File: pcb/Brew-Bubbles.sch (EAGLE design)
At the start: 10 parts, among them U1 GP1A57HR, U2 WEMOS-D1-MINI

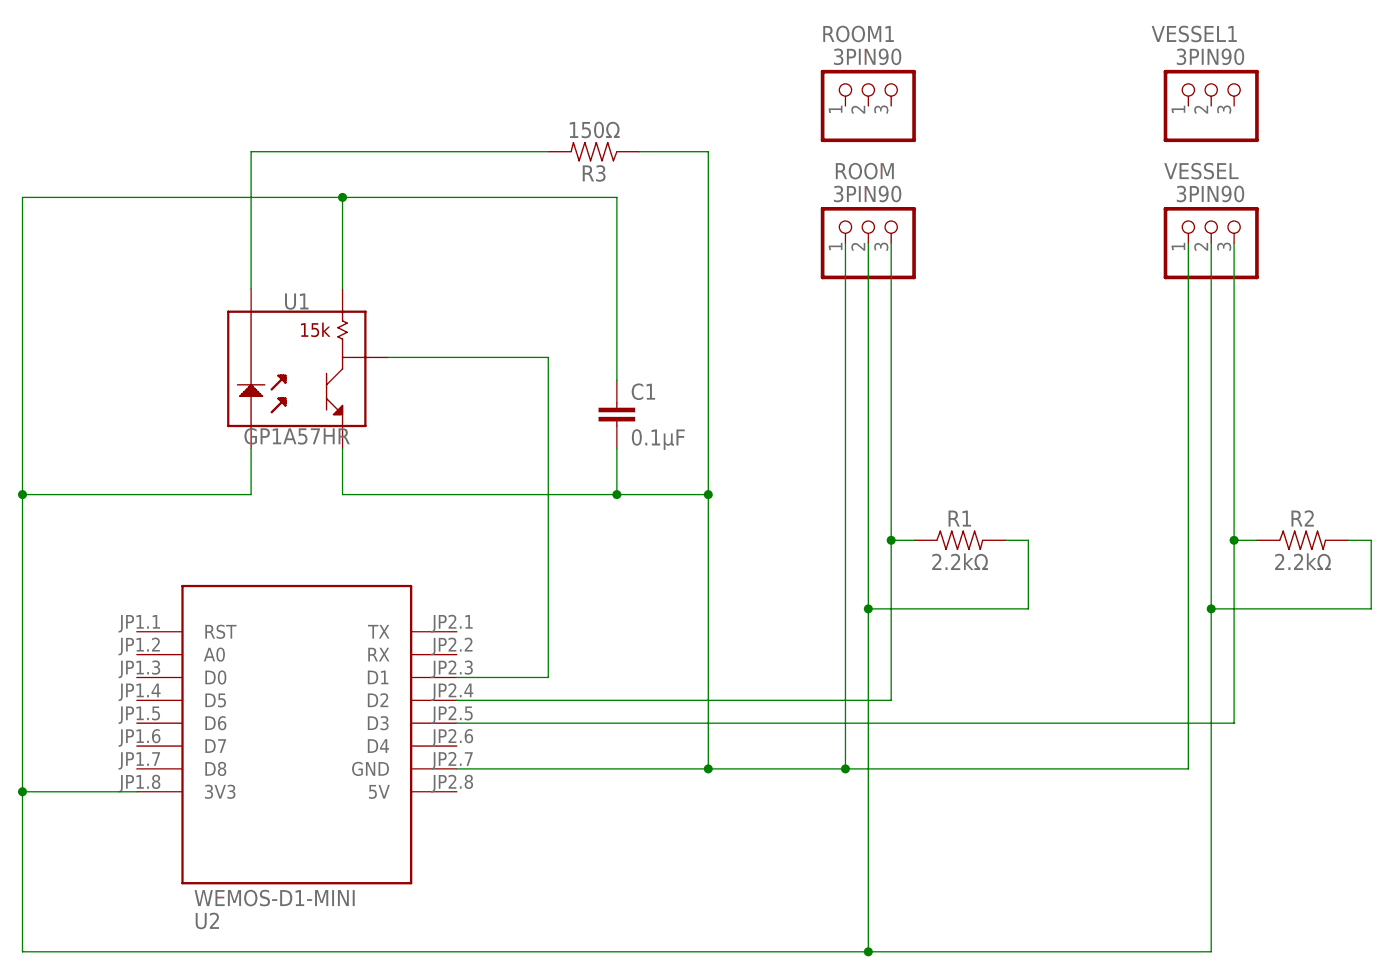
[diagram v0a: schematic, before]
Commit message: Add decoupling caps to 3v3 and 5v
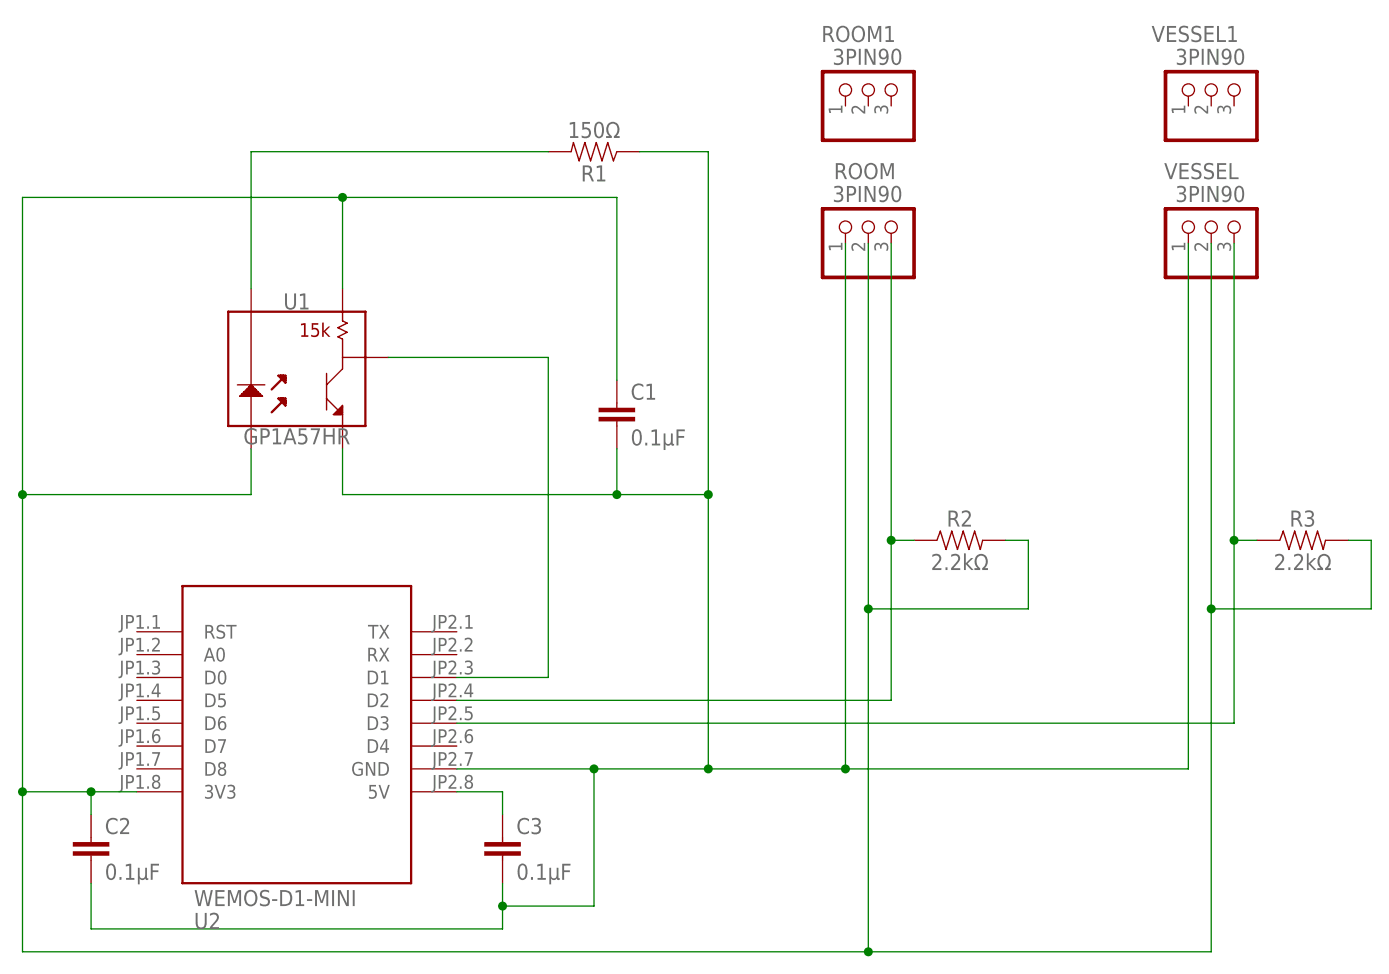
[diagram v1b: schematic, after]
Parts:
- added C2, C3: 0.1μF, rcl:C-EU025-024X044
- R1: value 2.2kΩ -> 150Ω
- R3: value 150Ω -> 2.2kΩ
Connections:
- new net 5V: C3.1, U2.5V
- net 3V3: now also C2.1, R3.2; no longer R1.2
- net D2: now also R2.1; no longer R1.1
- net D3: now also R3.1; no longer R2.1
- net GND: now also C2.2, C3.2, R1.1; no longer R3.1
- net PD1: now also R1.2; no longer R3.2
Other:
- moved on the sheet: R1, R2, R3
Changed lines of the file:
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@@
 <parts>
 <part name="U2" library="diy-modules" deviceset="WEMOS-D1-MINI-SHIELD" device="" value="WEMOS-D1-MINI"/>
-<part name="R1" library="SparkFun-Resistors" deviceset="330OHM" device="-HORIZ-1/10W-5%" value="2.2kΩ"/>
+<part name="R2" library="SparkFun-Resistors" deviceset="330OHM" device="-HORIZ-1/10W-5%" value="2.2kΩ"/>
 <part name="VESSEL" library="pinhead" library_urn="urn:adsk.eagle:library:325" deviceset="PINHD-1X3" device="/90" package3d_urn="urn:adsk.eagle:package:22459/2" value="3PIN90"/>
-<part name="R2" library="SparkFun-Resistors" deviceset="330OHM" device="-HORIZ-1/10W-5%" value="2.2kΩ"/>
+<part name="R3" library="SparkFun-Resistors" deviceset="330OHM" device="-HORIZ-1/10W-5%" value="2.2kΩ"/>
 <part name="U1" library="SparkFun-Sensors" deviceset="GP1A57HR" device=""/>
-<part name="R3" library="SparkFun-Resistors" deviceset="330OHM" device="-HORIZ-1/10W-5%" value="150Ω"/>
+<part name="R1" library="SparkFun-Resistors" deviceset="330OHM" device="-HORIZ-1/10W-5%" value="150Ω"/>
 <part name="ROOM" library="pinhead" library_urn="urn:adsk.eagle:library:325" deviceset="PINHD-1X3" device="/90" package3d_urn="urn:adsk.eagle:package:22459/2" value="3PIN90"/>
 <part name="FRAME1" library="frames" deviceset="LETTER_L" device=""/>
@@
 <part name="VESSEL1" library="pinhead" library_urn="urn:adsk.eagle:library:325" deviceset="PINHD-1X3" device="/90" package3d_urn="urn:adsk.eagle:package:22459/2" value="3PIN90"/>
 <part name="C1" library="rcl" library_urn="urn:adsk.eagle:library:334" deviceset="C-EU" device="025-024X044" package3d_urn="urn:adsk.eagle:package:23630/1" value="0.1μF"/>
+<part name="C3" library="rcl" library_urn="urn:adsk.eagle:library:334" deviceset="C-EU" device="025-024X044" package3d_urn="urn:adsk.eagle:package:23630/1" value="0.1μF"/>
+<part name="C2" library="rcl" library_urn="urn:adsk.eagle:library:334" deviceset="C-EU" device="025-024X044" package3d_urn="urn:adsk.eagle:package:23630/1" value="0.1μF"/>
 </parts>
 <sheets>
@@
 <attribute name="VALUE" x="6.35" y="33.02" size="1.778" layer="96"/>
 </instance>
-<instance part="R1" gate="G$1" x="91.44" y="73.66" smashed="yes">
+<instance part="R2" gate="G$1" x="91.44" y="73.66" smashed="yes">
 <attribute name="NAME" x="91.44" y="75.184" size="1.778" layer="95" font="vector" align="bottom-center"/>
 <attribute name="VALUE" x="91.44" y="72.136" size="1.778" layer="96" font="vector" align="top-center"/>
@@
 <attribute name="NAME" x="122.428" y="115.57" size="1.778" layer="95" rot="R180"/>
 </instance>
-<instance part="R2" gate="G$1" x="129.54" y="73.66" smashed="yes">
+<instance part="R3" gate="G$1" x="129.54" y="73.66" smashed="yes">
 <attribute name="NAME" x="129.54" y="75.184" size="1.778" layer="95" font="vector" align="bottom-center"/>
 <attribute name="VALUE" x="129.54" y="72.136" size="1.778" layer="96" font="vector" align="top-center"/>
@@
 <attribute name="VALUE" x="17.78" y="86.106" size="1.778" layer="96" font="vector" align="top-center"/>
 </instance>
-<instance part="R3" gate="G$1" x="50.8" y="116.84" smashed="yes" rot="R180">
+<instance part="R1" gate="G$1" x="50.8" y="116.84" smashed="yes" rot="R180">
 <attribute name="NAME" x="50.8" y="115.316" size="1.778" layer="95" font="vector" rot="R180" align="bottom-center"/>
 <attribute name="VALUE" x="50.8" y="118.364" size="1.778" layer="96" font="vector" rot="R180" align="top-center"/>
@@
 <attribute name="VALUE" x="54.864" y="84.201" size="1.778" layer="96"/>
 </instance>
+<instance part="C3" gate="G$1" x="40.64" y="40.64" smashed="yes">
+<attribute name="NAME" x="42.164" y="41.021" size="1.778" layer="95"/>
+<attribute name="VALUE" x="42.164" y="35.941" size="1.778" layer="96"/>
+</instance>
+<instance part="C2" gate="G$1" x="-5.08" y="40.64" smashed="yes">
+<attribute name="NAME" x="-3.556" y="41.021" size="1.778" layer="95"/>
+<attribute name="VALUE" x="-3.556" y="35.941" size="1.778" layer="96"/>
+</instance>
 </instances>
 <busses>
@@
 <wire x1="12.7" y1="83.82" x2="12.7" y2="78.74" width="0.1524" layer="91"/>
 <pinref part="U2" gate="G$1" pin="3V3"/>
-<wire x1="0" y1="45.72" x2="-12.7" y2="45.72" width="0.1524" layer="91"/>
+<wire x1="0" y1="45.72" x2="-5.08" y2="45.72" width="0.1524" layer="91"/>
+<wire x1="-5.08" y1="45.72" x2="-12.7" y2="45.72" width="0.1524" layer="91"/>
 <wire x1="-12.7" y1="45.72" x2="-12.7" y2="78.74" width="0.1524" layer="91"/>
 <wire x1="-12.7" y1="78.74" x2="-12.7" y2="111.76" width="0.1524" layer="91"/>
@@
 <pinref part="U1" gate="G$1" pin="3"/>
 <wire x1="22.86" y1="111.76" x2="22.86" y2="101.6" width="0.1524" layer="91"/>
+<pinref part="R3" gate="G$1" pin="2"/>
 <pinref part="R2" gate="G$1" pin="2"/>
-<pinref part="R1" gate="G$1" pin="2"/>
 <pinref part="VESSEL" gate="A" pin="2"/>
 <pinref part="ROOM" gate="A" pin="2"/>
@@
 <pinref part="C1" gate="G$1" pin="1"/>
 <wire x1="53.34" y1="111.76" x2="53.34" y2="91.44" width="0.1524" layer="91"/>
+<pinref part="C2" gate="G$1" pin="1"/>
+<wire x1="-5.08" y1="43.18" x2="-5.08" y2="45.72" width="0.1524" layer="91"/>
+<junction x="-5.08" y="45.72"/>
 </segment>
 </net>
@@
 <segment>
 <pinref part="U2" gate="G$1" pin="D2"/>
-<pinref part="R1" gate="G$1" pin="1"/>
+<pinref part="R2" gate="G$1" pin="1"/>
 <pinref part="ROOM" gate="A" pin="3"/>
 <wire x1="83.82" y1="55.88" x2="83.82" y2="73.66" width="0.1524" layer="91"/>
@@
 <segment>
 <pinref part="U2" gate="G$1" pin="D3"/>
-<pinref part="R2" gate="G$1" pin="1"/>
+<pinref part="R3" gate="G$1" pin="1"/>
 <pinref part="VESSEL" gate="A" pin="3"/>
 <wire x1="35.56" y1="53.34" x2="121.92" y2="53.34" width="0.1524" layer="91"/>
@@
 <pinref part="U2" gate="G$1" pin="GND"/>
 <pinref part="VESSEL" gate="A" pin="1"/>
-<pinref part="R3" gate="G$1" pin="1"/>
+<pinref part="R1" gate="G$1" pin="1"/>
 <pinref part="U1" gate="G$1" pin="5"/>
 <wire x1="22.86" y1="83.82" x2="22.86" y2="78.74" width="0.1524" layer="91"/>
@@
 <wire x1="63.5" y1="48.26" x2="78.74" y2="48.26" width="0.1524" layer="91"/>
 <wire x1="78.74" y1="48.26" x2="116.84" y2="48.26" width="0.1524" layer="91"/>
-<wire x1="35.56" y1="48.26" x2="63.5" y2="48.26" width="0.1524" layer="91"/>
+<wire x1="35.56" y1="48.26" x2="50.8" y2="48.26" width="0.1524" layer="91"/>
 <junction x="63.5" y="48.26"/>
 <pinref part="ROOM" gate="A" pin="1"/>
+<wire x1="50.8" y1="48.26" x2="63.5" y2="48.26" width="0.1524" layer="91"/>
 <wire x1="78.74" y1="48.26" x2="78.74" y2="106.68" width="0.1524" layer="91"/>
 <junction x="78.74" y="48.26"/>
@@
 <wire x1="53.34" y1="83.82" x2="53.34" y2="78.74" width="0.1524" layer="91"/>
 <junction x="53.34" y="78.74"/>
+<pinref part="C3" gate="G$1" pin="2"/>
+<wire x1="40.64" y1="35.56" x2="40.64" y2="33.02" width="0.1524" layer="91"/>
+<wire x1="40.64" y1="33.02" x2="50.8" y2="33.02" width="0.1524" layer="91"/>
+<wire x1="50.8" y1="33.02" x2="50.8" y2="48.26" width="0.1524" layer="91"/>
+<junction x="50.8" y="48.26"/>
+<pinref part="C2" gate="G$1" pin="2"/>
+<wire x1="-5.08" y1="35.56" x2="-5.08" y2="30.48" width="0.1524" layer="91"/>
+<wire x1="-5.08" y1="30.48" x2="40.64" y2="30.48" width="0.1524" layer="91"/>
+<wire x1="40.64" y1="30.48" x2="40.64" y2="33.02" width="0.1524" layer="91"/>
+<junction x="40.64" y="33.02"/>
 </segment>
 </net>
@@
 <segment>
 <pinref part="U1" gate="G$1" pin="2"/>
-<pinref part="R3" gate="G$1" pin="2"/>
+<pinref part="R1" gate="G$1" pin="2"/>
 <wire x1="45.72" y1="116.84" x2="12.7" y2="116.84" width="0.1524" layer="91"/>
 <wire x1="12.7" y1="116.84" x2="12.7" y2="101.6" width="0.1524" layer="91"/>
 </segment>
 </net>
+<net name="5V" class="0">
+<segment>
+<pinref part="U2" gate="G$1" pin="5V"/>
+<wire x1="35.56" y1="45.72" x2="40.64" y2="45.72" width="0.1524" layer="91"/>
+<pinref part="C3" gate="G$1" pin="1"/>
+<wire x1="40.64" y1="45.72" x2="40.64" y2="43.18" width="0.1524" layer="91"/>
+</segment>
+</net>
